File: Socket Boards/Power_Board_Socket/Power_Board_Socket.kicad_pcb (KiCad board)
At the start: 2 copper layers, 38 x 47.3 mm, 41 parts

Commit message: Fixed paths of module boards
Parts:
- J1: footprint HeepoMind_PcbLib:Power_Board_Header_Conn_2.54mm -> X-MODs_PcbLib:Power_Board_Header_Conn_2.54mm
- J2: footprint HeepoMind_PcbLib:Power_Board_Socket_Conn_1.27mm -> X-MODs_PcbLib:Power_Board_Socket_Conn_1.27mm
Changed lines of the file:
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@@
 		)
 	)
-	(footprint "HeepoMind_PcbLib:Power_Board_Header_Conn_2.54mm"
+	(footprint "X-MODs_PcbLib:Power_Board_Header_Conn_2.54mm"
 		(layer "F.Cu")
 		(at 136.99 111.93)
@@
 			)
 		)
-		(property "Footprint" "HeepoMind_PcbLib:Power_Board_Header_Conn_2.54mm"
+		(property "Footprint" "X-MODs_PcbLib:Power_Board_Header_Conn_2.54mm"
 			(at 0 -9 0)
 			(unlocked yes)
@@
 			(pintype "passive")
 		)
-		(model "C:/Users/Alex/OneDrive/ESL/HEEPoMind/ALEX/Libraries/3D Models/Headers/PinHeader_1x16_P2.54mm_Vertical.step"
+		(model "C:/Users/Alex/OneDrive/ESL/X-MODs/Libraries/3D Models/Headers/PinHeader_1x16_P2.54mm_Vertical.step"
 			(offset
 				(xyz 17.61 19.05 -1.58)
@@
 			)
 		)
-		(model "C:/Users/Alex/OneDrive/ESL/HEEPoMind/ALEX/Libraries/3D Models/Headers/PinHeader_1x18_P2.54mm_Vertical.step"
+		(model "C:/Users/Alex/OneDrive/ESL/X-MODs/Libraries/3D Models/Headers/PinHeader_1x18_P2.54mm_Vertical.step"
 			(offset
 				(xyz -17.61 21.59 -1.58)
@@
 		)
 	)
-	(footprint "HeepoMind_PcbLib:Power_Board_Socket_Conn_1.27mm"
+	(footprint "X-MODs_PcbLib:Power_Board_Socket_Conn_1.27mm"
 		(layer "F.Cu")
 		(at 136.99 111.93)
@@
 			)
 		)
-		(property "Footprint" "HeepoMind_PcbLib:Power_Board_Socket_Conn_1.27mm"
+		(property "Footprint" "X-MODs_PcbLib:Power_Board_Socket_Conn_1.27mm"
 			(at -1.34 -5.55 0)
 			(unlocked yes)
@@
 			)
 		)
-		(model "C:/Users/Alex/OneDrive/ESL/HEEPoMind/ALEX/Libraries/3D Models/Flexypin/flexypin.step"
+		(model "C:/Users/Alex/OneDrive/ESL/X-MODs/Libraries/3D Models/Flexypin/flexypin.step"
 			(offset
 				(xyz 8.825 4.445 0)
@@
 			)
 		)
-		(model "C:/Users/Alex/OneDrive/ESL/HEEPoMind/ALEX/Libraries/3D Models/Flexypin/flexypin.step"
+		(model "C:/Users/Alex/OneDrive/ESL/X-MODs/Libraries/3D Models/Flexypin/flexypin.step"
 			(offset
 				(xyz 8.825 3.175 0)
@@
 			)
 		)
-		(model "C:/Users/Alex/OneDrive/ESL/HEEPoMind/ALEX/Libraries/3D Models/Flexypin/flexypin.step"
+		(model "C:/Users/Alex/OneDrive/ESL/X-MODs/Libraries/3D Models/Flexypin/flexypin.step"
 			(offset
 				(xyz 8.825 1.905 0)
@@
 			)
 		)
-		(model "C:/Users/Alex/OneDrive/ESL/HEEPoMind/ALEX/Libraries/3D Models/Flexypin/flexypin.step"
+		(model "C:/Users/Alex/OneDrive/ESL/X-MODs/Libraries/3D Models/Flexypin/flexypin.step"
 			(offset
 				(xyz 8.825 0.635 0)
@@
 			)
 		)
-		(model "C:/Users/Alex/OneDrive/ESL/HEEPoMind/ALEX/Libraries/3D Models/Flexypin/flexypin.step"
+		(model "C:/Users/Alex/OneDrive/ESL/X-MODs/Libraries/3D Models/Flexypin/flexypin.step"
 			(offset
 				(xyz 8.825 -0.635 0)
@@
 			)
 		)
-		(model "C:/Users/Alex/OneDrive/ESL/HEEPoMind/ALEX/Libraries/3D Models/Flexypin/flexypin.step"
+		(model "C:/Users/Alex/OneDrive/ESL/X-MODs/Libraries/3D Models/Flexypin/flexypin.step"
 			(offset
 				(xyz 8.825 -1.905 0)
@@
 			)
 		)
-		(model "C:/Users/Alex/OneDrive/ESL/HEEPoMind/ALEX/Libraries/3D Models/Flexypin/flexypin.step"
+		(model "C:/Users/Alex/OneDrive/ESL/X-MODs/Libraries/3D Models/Flexypin/flexypin.step"
 			(offset
 				(xyz 8.825 -3.175 0)
@@
 			)
 		)
-		(model "C:/Users/Alex/OneDrive/ESL/HEEPoMind/ALEX/Libraries/3D Models/Flexypin/flexypin.step"
+		(model "C:/Users/Alex/OneDrive/ESL/X-MODs/Libraries/3D Models/Flexypin/flexypin.step"
 			(offset
 				(xyz 8.825 -4.445 0)
@@
 			)
 		)
-		(model "C:/Users/Alex/OneDrive/ESL/HEEPoMind/ALEX/Libraries/3D Models/Flexypin/flexypin.step"
+		(model "C:/Users/Alex/OneDrive/ESL/X-MODs/Libraries/3D Models/Flexypin/flexypin.step"
 			(offset
 				(xyz -8.825 4.445 0)
@@
 			)
 		)
-		(model "C:/Users/Alex/OneDrive/ESL/HEEPoMind/ALEX/Libraries/3D Models/Flexypin/flexypin.step"
+		(model "C:/Users/Alex/OneDrive/ESL/X-MODs/Libraries/3D Models/Flexypin/flexypin.step"
 			(offset
 				(xyz -8.825 3.175 0)
@@
 			)
 		)
-		(model "C:/Users/Alex/OneDrive/ESL/HEEPoMind/ALEX/Libraries/3D Models/Flexypin/flexypin.step"
+		(model "C:/Users/Alex/OneDrive/ESL/X-MODs/Libraries/3D Models/Flexypin/flexypin.step"
 			(offset
 				(xyz -8.825 1.905 0)
@@
 			)
 		)
-		(model "C:/Users/Alex/OneDrive/ESL/HEEPoMind/ALEX/Libraries/3D Models/Flexypin/flexypin.step"
+		(model "C:/Users/Alex/OneDrive/ESL/X-MODs/Libraries/3D Models/Flexypin/flexypin.step"
 			(offset
 				(xyz -8.825 0.635 0)
@@
 			)
 		)
-		(model "C:/Users/Alex/OneDrive/ESL/HEEPoMind/ALEX/Libraries/3D Models/Flexypin/flexypin.step"
+		(model "C:/Users/Alex/OneDrive/ESL/X-MODs/Libraries/3D Models/Flexypin/flexypin.step"
 			(offset
 				(xyz -8.825 -0.635 0)
@@
 			)
 		)
-		(model "C:/Users/Alex/OneDrive/ESL/HEEPoMind/ALEX/Libraries/3D Models/Flexypin/flexypin.step"
+		(model "C:/Users/Alex/OneDrive/ESL/X-MODs/Libraries/3D Models/Flexypin/flexypin.step"
 			(offset
 				(xyz -8.825 -1.905 0)
@@
 			)
 		)
-		(model "C:/Users/Alex/OneDrive/ESL/HEEPoMind/ALEX/Libraries/3D Models/Flexypin/flexypin.step"
+		(model "C:/Users/Alex/OneDrive/ESL/X-MODs/Libraries/3D Models/Flexypin/flexypin.step"
 			(offset
 				(xyz -8.825 -3.175 0)
@@
 			)
 		)
-		(model "C:/Users/Alex/OneDrive/ESL/HEEPoMind/ALEX/Libraries/3D Models/Flexypin/flexypin.step"
+		(model "C:/Users/Alex/OneDrive/ESL/X-MODs/Libraries/3D Models/Flexypin/flexypin.step"
 			(offset
 				(xyz -8.825 -4.445 0)
@@
 			)
 		)
-		(model "C:/Users/Alex/OneDrive/ESL/HEEPoMind/ALEX/Libraries/3D Models/Flexypin/flexypin.step"
+		(model "C:/Users/Alex/OneDrive/ESL/X-MODs/Libraries/3D Models/Flexypin/flexypin.step"
 			(offset
 				(xyz -5.08 7.7 0)
@@
 			)
 		)
-		(model "C:/Users/Alex/OneDrive/ESL/HEEPoMind/ALEX/Libraries/3D Models/Flexypin/flexypin.step"
+		(model "C:/Users/Alex/OneDrive/ESL/X-MODs/Libraries/3D Models/Flexypin/flexypin.step"
 			(offset
 				(xyz -3.81 7.7 0)
@@
 			)
 		)
-		(model "C:/Users/Alex/OneDrive/ESL/HEEPoMind/ALEX/Libraries/3D Models/Flexypin/flexypin.step"
+		(model "C:/Users/Alex/OneDrive/ESL/X-MODs/Libraries/3D Models/Flexypin/flexypin.step"
 			(offset
 				(xyz -2.54 7.7 0)
@@
 			)
 		)
-		(model "C:/Users/Alex/OneDrive/ESL/HEEPoMind/ALEX/Libraries/3D Models/Flexypin/flexypin.step"
+		(model "C:/Users/Alex/OneDrive/ESL/X-MODs/Libraries/3D Models/Flexypin/flexypin.step"
 			(offset
 				(xyz -1.27 7.7 0)
@@
 			)
 		)
-		(model "C:/Users/Alex/OneDrive/ESL/HEEPoMind/ALEX/Libraries/3D Models/Flexypin/flexypin.step"
+		(model "C:/Users/Alex/OneDrive/ESL/X-MODs/Libraries/3D Models/Flexypin/flexypin.step"
 			(offset
 				(xyz 0 7.7 0)
@@
 			)
 		)
-		(model "C:/Users/Alex/OneDrive/ESL/HEEPoMind/ALEX/Libraries/3D Models/Flexypin/flexypin.step"
+		(model "C:/Users/Alex/OneDrive/ESL/X-MODs/Libraries/3D Models/Flexypin/flexypin.step"
 			(offset
 				(xyz 1.27 7.7 0)
@@
 			)
 		)
-		(model "C:/Users/Alex/OneDrive/ESL/HEEPoMind/ALEX/Libraries/3D Models/Flexypin/flexypin.step"
+		(model "C:/Users/Alex/OneDrive/ESL/X-MODs/Libraries/3D Models/Flexypin/flexypin.step"
 			(offset
 				(xyz 2.54 7.7 0)
@@
 			)
 		)
-		(model "C:/Users/Alex/OneDrive/ESL/HEEPoMind/ALEX/Libraries/3D Models/Flexypin/flexypin.step"
+		(model "C:/Users/Alex/OneDrive/ESL/X-MODs/Libraries/3D Models/Flexypin/flexypin.step"
 			(offset
 				(xyz 3.81 7.7 0)
@@
 			)
 		)
-		(model "C:/Users/Alex/OneDrive/ESL/HEEPoMind/ALEX/Libraries/3D Models/Flexypin/flexypin.step"
+		(model "C:/Users/Alex/OneDrive/ESL/X-MODs/Libraries/3D Models/Flexypin/flexypin.step"
 			(offset
 				(xyz 5.08 7.7 0)
@@
 			)
 		)
-		(model "C:/Users/Alex/OneDrive/ESL/HEEPoMind/ALEX/Libraries/3D Models/Flexypin/flexypin.step"
+		(model "C:/Users/Alex/OneDrive/ESL/X-MODs/Libraries/3D Models/Flexypin/flexypin.step"
 			(offset
 				(xyz -5.08 -7.7 0)
@@
 			)
 		)
-		(model "C:/Users/Alex/OneDrive/ESL/HEEPoMind/ALEX/Libraries/3D Models/Flexypin/flexypin.step"
+		(model "C:/Users/Alex/OneDrive/ESL/X-MODs/Libraries/3D Models/Flexypin/flexypin.step"
 			(offset
 				(xyz -3.81 -7.7 0)
@@
 			)
 		)
-		(model "C:/Users/Alex/OneDrive/ESL/HEEPoMind/ALEX/Libraries/3D Models/Flexypin/flexypin.step"
+		(model "C:/Users/Alex/OneDrive/ESL/X-MODs/Libraries/3D Models/Flexypin/flexypin.step"
 			(offset
 				(xyz -2.54 -7.7 0)
@@
 			)
 		)
-		(model "C:/Users/Alex/OneDrive/ESL/HEEPoMind/ALEX/Libraries/3D Models/Flexypin/flexypin.step"
+		(model "C:/Users/Alex/OneDrive/ESL/X-MODs/Libraries/3D Models/Flexypin/flexypin.step"
 			(offset
 				(xyz -1.27 -7.7 0)
@@
 			)
 		)
-		(model "C:/Users/Alex/OneDrive/ESL/HEEPoMind/ALEX/Libraries/3D Models/Flexypin/flexypin.step"
+		(model "C:/Users/Alex/OneDrive/ESL/X-MODs/Libraries/3D Models/Flexypin/flexypin.step"
 			(offset
 				(xyz 0 -7.7 0)
@@
 			)
 		)
-		(model "C:/Users/Alex/OneDrive/ESL/HEEPoMind/ALEX/Libraries/3D Models/Flexypin/flexypin.step"
+		(model "C:/Users/Alex/OneDrive/ESL/X-MODs/Libraries/3D Models/Flexypin/flexypin.step"
 			(offset
 				(xyz 1.27 -7.7 0)
@@
 			)
 		)
-		(model "C:/Users/Alex/OneDrive/ESL/HEEPoMind/ALEX/Libraries/3D Models/Flexypin/flexypin.step"
+		(model "C:/Users/Alex/OneDrive/ESL/X-MODs/Libraries/3D Models/Flexypin/flexypin.step"
 			(offset
 				(xyz 2.54 -7.7 0)
@@
 			)
 		)
-		(model "C:/Users/Alex/OneDrive/ESL/HEEPoMind/ALEX/Libraries/3D Models/Flexypin/flexypin.step"
+		(model "C:/Users/Alex/OneDrive/ESL/X-MODs/Libraries/3D Models/Flexypin/flexypin.step"
 			(offset
 				(xyz 3.81 -7.7 0)
@@
 			)
 		)
-		(model "C:/Users/Alex/OneDrive/ESL/HEEPoMind/ALEX/Libraries/3D Models/Flexypin/flexypin.step"
+		(model "C:/Users/Alex/OneDrive/ESL/X-MODs/Libraries/3D Models/Flexypin/flexypin.step"
 			(offset
 				(xyz 5.08 -7.7 0)

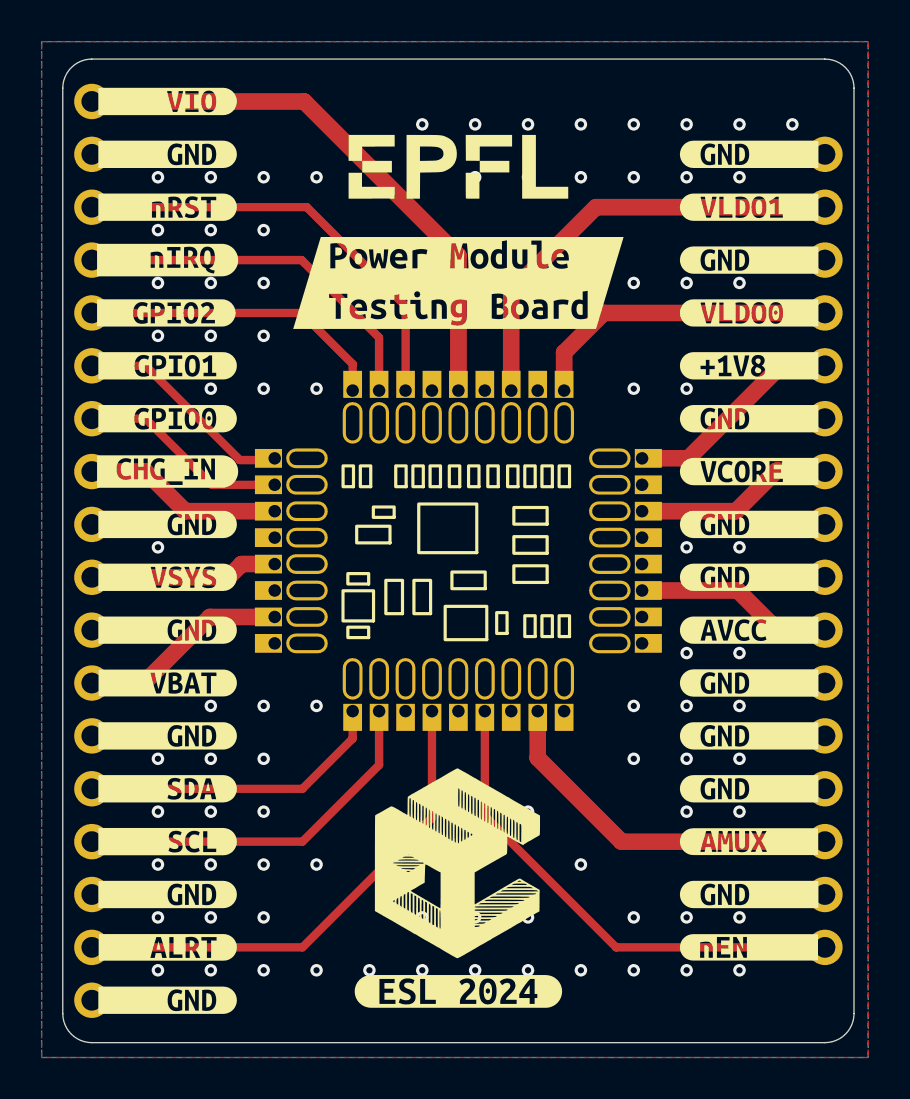
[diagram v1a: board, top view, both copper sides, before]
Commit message: Added via stitching to the socket boards
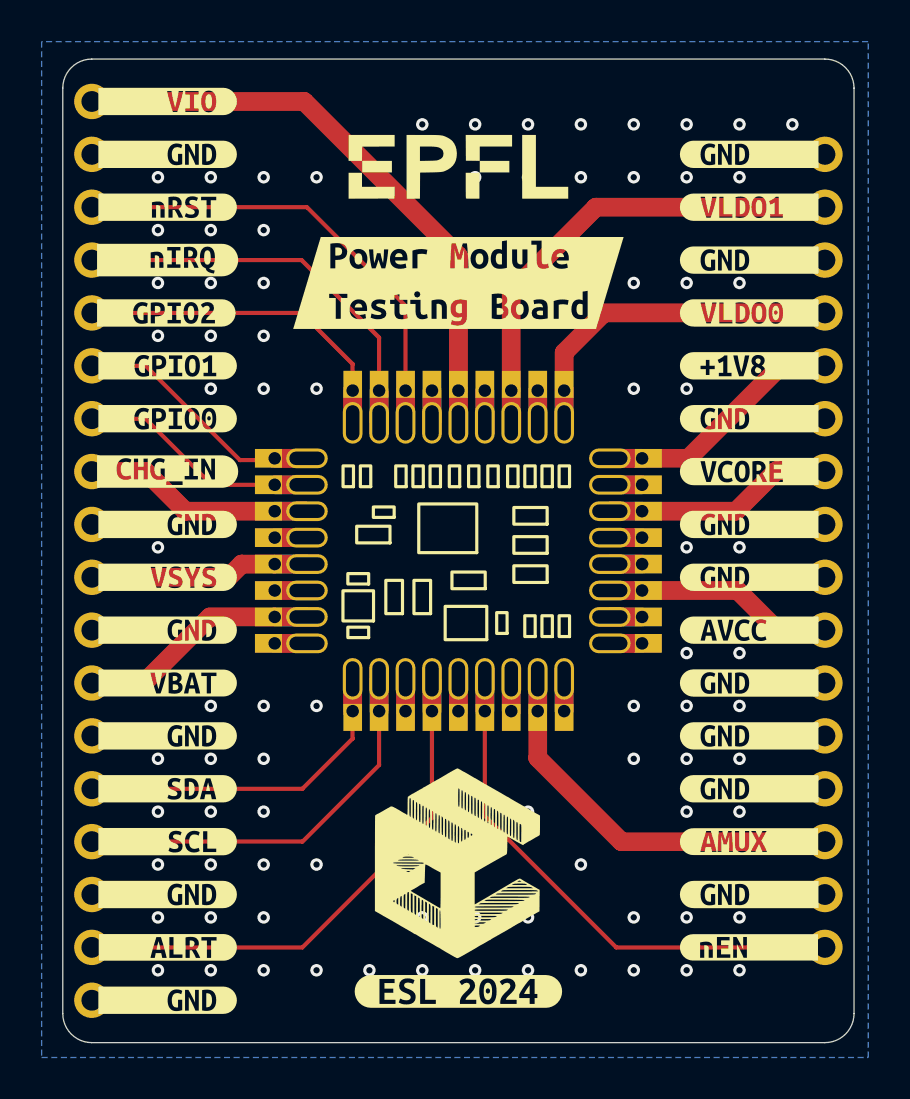
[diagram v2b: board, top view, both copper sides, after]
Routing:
- net GND: track 0.00 -> 46.5 mm
- net /VSYS: track 9.00 -> 12.1 mm
- net /VCORE: track 9.56 -> 12.7 mm
- net /VBAT: track 10.1 -> 13.2 mm
- net /GPIO1: track 10.7 -> 13.8 mm
- net /GPIO0: track 10.1 -> 13.2 mm
- net /CHG_IN: track 9.52 -> 12.6 mm
- net /AVCC: track 9.52 -> 12.6 mm
- net /+1V8: track 10.6 -> 13.7 mm
- net nEN: track 24.0 -> 27.1 mm
- net VLDO1: track 21.4 -> 24.5 mm
- net VLDO0: track 15.1 -> 18.2 mm
- net AMUX: track 17.7 -> 20.8 mm
- net /nRST: track 21.1 -> 24.2 mm
- net /nIRQ: track 17.9 -> 21.0 mm
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- added copper zone on In1.Cu, net GND
- added copper zone on In2.Cu, net GND
- removed copper zone on F.Cu, net GND
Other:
- copper layers 2 -> 4
